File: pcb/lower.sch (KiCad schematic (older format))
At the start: 42 parts, among them J1 MALE, J10 TC2030_NL, J11 STANDOFF, J12 STANDOFF, J13 STANDOFF, J14 STANDOFF, J2 FEMALE, J3 MALE, J4 FEMALE, J5 MALE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

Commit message: 15 → 22 Ω for safety and to avoid clipping
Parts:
- R16: value 15 0.5W -> 22 0.5W; LCSC Part # C40361 -> C70404; MPN 2010W2F150JT4E -> 2010W2F220JT4S
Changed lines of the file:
@@
 P 8500 4650
 F 0 "R16" V 8295 4650 50  0000 C CNN
-F 1 "15 0.5W" V 8386 4650 50  0000 C CNN
+F 1 "22 0.5W" V 8386 4650 50  0000 C CNN
 F 2 "Resistor_SMD:R_2010_5025Metric" H 8500 4650 50  0001 C CNN
-F 3 "https://datasheet.lcsc.com/szlcsc/Uniroyal-Elec-2010W2F150JT4E_C40361.pdf" H 8500 4650 50  0001 C CNN
-F 4 "C40361" H 8500 4650 50  0001 C CNN "LCSC Part #"
-F 5 "2010W2F150JT4E" H 8500 4650 50  0001 C CNN "MPN"
+F 3 "https://datasheet.lcsc.com/szlcsc/Uniroyal-Elec-2010W2F220JT4S_C70404.pdf" H 8500 4650 50  0001 C CNN
+F 4 "C70404" H 8500 4650 50  0001 C CNN "LCSC Part #"
+F 5 "2010W2F220JT4S" H 8500 4650 50  0001 C CNN "MPN"
 F 6 "Uniroyal Elec" H 8500 4650 50  0001 C CNN "Manufacturer"
 F 7 "2010" H 8500 4650 50  0001 C CNN "Package"

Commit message: Change to parts available for JLCPCB PCBA
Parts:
- C1: value 0.1u -> 100n; LCSC Part # C60474 -> C1525; MPN CC0402KRX7R7BB104 -> CL05B104KO5NNNC; Manufacturer YAGEO -> Samsung Electro-Mechanics
- C2, C3: LCSC Part # C277478 -> C1547; MPN CC0201JRNPO9BN120 -> 0402CG120J500NT; Manufacturer YAGEO -> Guangdong Fenghua Advanced Tech
- R1, R10, R11, R12, R13, R14, R15, R2, R3, R4, R5, R6, R7, R8: LCSC Part # C114949 -> C25117; MPN RC0402JR-07470RL -> 0402WGF4700TCE; Manufacturer YAGEO -> Uniroyal Elec
- R9: LCSC Part # C102629 -> C25744; MPN RC0402JR-0710KL -> 0402WGF1002TCE; Manufacturer RALEC -> Uniroyal Elec
- Y1: Package (none) -> SMD-3225_4P

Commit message: Make fields compatible with JLCPCB BOM plugin
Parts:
- BZ1: JLCPCB BOM (none) -> False; LCSC Part (none) -> C94598; LCSC Part # C94598 -> (none)
- C1: LCSC Part (none) -> C1525; LCSC Part # C1525 -> (none)
- C2, C3: LCSC Part (none) -> C1547; LCSC Part # C1547 -> (none)
- D1, D2, D3, D4: LCSC Part (none) -> C194323; LCSC Part # C194323 -> (none)
- D5: LCSC Part (none) -> C60580; LCSC Part # C60580 -> (none)
- J1, J3, J5, J7: JLCPCB BOM (none) -> False; LCSC Part (none) -> C239333; LCSC Part # C239333 -> (none)
- J10, J11, J12, J13, J14, J9: JLCPCB BOM (none) -> False
- J2, J4, J6, J8: JLCPCB BOM (none) -> False; LCSC Part (none) -> C239353; LCSC Part # C239353 -> (none)
- Q1: LCSC Part (none) -> C8667; LCSC Part # C8667 -> (none)
- R1, R10, R11, R12, R13, R14, R15, R2, R3, R4, R5, R6, R7, R8: LCSC Part (none) -> C25117; LCSC Part # C25117 -> (none)
- R16: LCSC Part (none) -> C70404; LCSC Part # C70404 -> (none)
- R9: LCSC Part (none) -> C25744; LCSC Part # C25744 -> (none)
- U3: LCSC Part (none) -> C783592; LCSC Part # C783592 -> (none)
- Y1: LCSC Part (none) -> C12668; LCSC Part # C12668 -> (none)

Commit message: Fix: Wrong pin numbering of transistor
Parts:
- Q1: symbol Transistor_BJT:PN2222A -> node:PMBT3904
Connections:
- net GNDB: now also Q1.2 (E); no longer Q1.1 (E)
- net at R15.1: now also Q1.1 (B); no longer Q1.2 (B)
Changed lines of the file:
@@
 	8350 5100 8500 5100
 $Comp
-L Transistor_BJT:PN2222A Q1
+L node:PMBT3904 Q1
 U 1 1 5F9890BA
 P 8400 5500

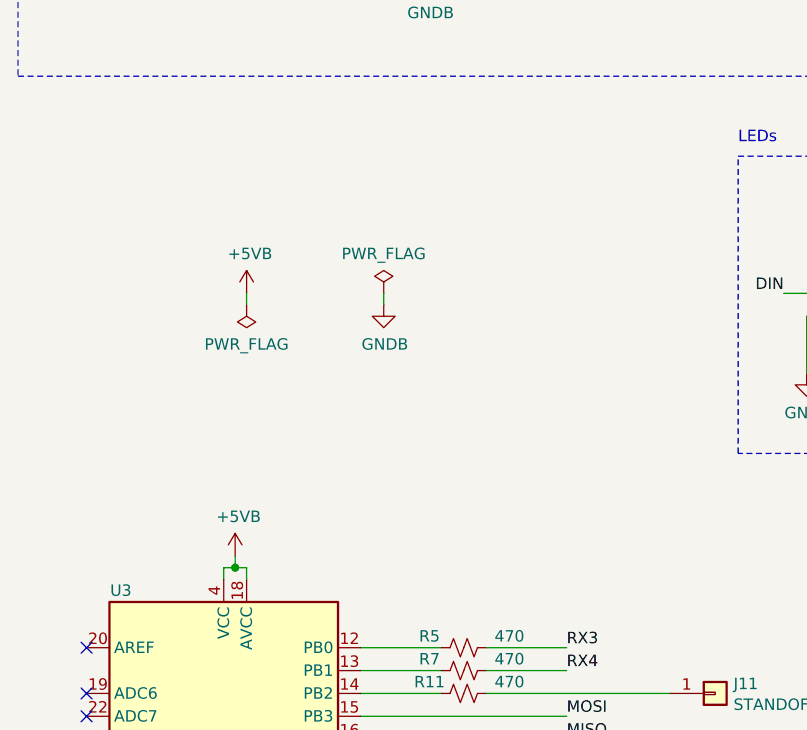
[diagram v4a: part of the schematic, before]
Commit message: Specify and wire up Schottky diode
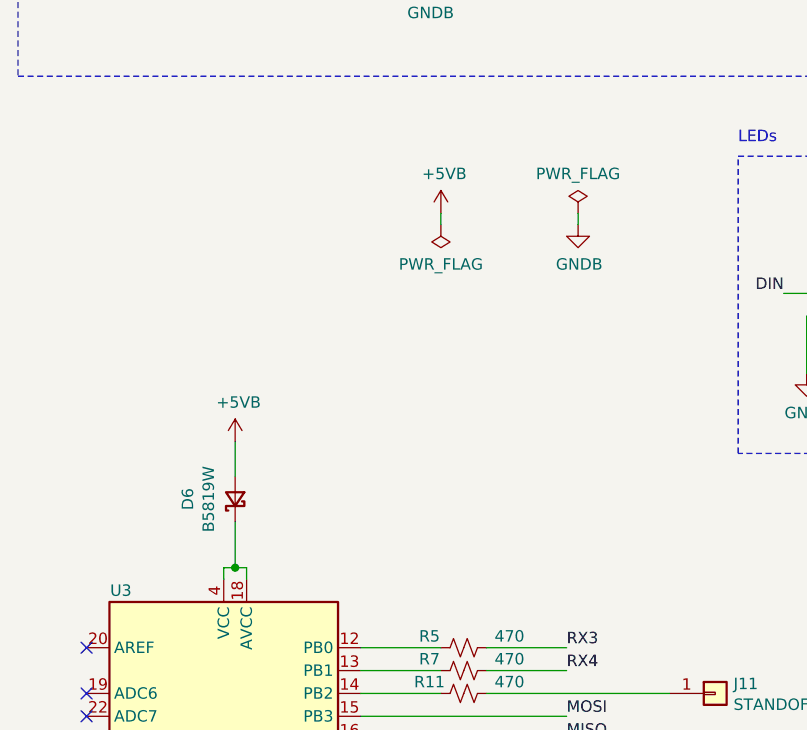
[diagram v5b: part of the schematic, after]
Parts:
- added D6: B5819W, Diode_SMD:D_SOD-123, symbol Device:D_Schottky_Small
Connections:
- net +5VB: now also D6.2 (A); no longer U3.18 (AVCC), U3.4 (VCC), U3.6 (VCC)
- new net: D6.1 (K), U3.18 (AVCC), U3.4 (VCC), U3.6 (VCC)
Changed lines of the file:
@@
 RX4
-Wire Wire Line
-	1550 4300 1550 4350
 Wire Wire Line
 	2450 4900 2100 4900
@@
 L node:+5VB #PWR0101
 U 1 1 5F8748FF
-P 1550 4300
-F 0 "#PWR0101" H 1550 4150 50  0001 C CNN
-F 1 "+5VB" H 1565 4473 50  0000 C CNN
-F 2 "" H 1550 4300 50  0001 C CNN
-F 3 "" H 1550 4300 50  0001 C CNN
-	1    1550 4300
+P 1550 3800
+F 0 "#PWR0101" H 1550 3650 50  0001 C CNN
+F 1 "+5VB" H 1565 3973 50  0000 C CNN
+F 2 "" H 1550 3800 50  0001 C CNN
+F 3 "" H 1550 3800 50  0001 C CNN
+	1    1550 3800
 	1    0    0    -1
 $EndComp
@@
 L power:PWR_FLAG #FLG0101
 U 1 1 5F887FE3
-P 2200 3150
-F 0 "#FLG0101" H 2200 3225 50  0001 C CNN
-F 1 "PWR_FLAG" H 2200 3323 50  0000 C CNN
-F 2 "" H 2200 3150 50  0001 C CNN
-F 3 "~" H 2200 3150 50  0001 C CNN
-	1    2200 3150
+P 3050 2800
+F 0 "#FLG0101" H 3050 2875 50  0001 C CNN
+F 1 "PWR_FLAG" H 3050 2973 50  0000 C CNN
+F 2 "" H 3050 2800 50  0001 C CNN
+F 3 "~" H 3050 2800 50  0001 C CNN
+	1    3050 2800
 	1    0    0    -1
 $EndComp
@@
 L node:+5VB #PWR0128
 U 1 1 5F888530
-P 1600 3150
-F 0 "#PWR0128" H 1600 3000 50  0001 C CNN
-F 1 "+5VB" H 1615 3323 50  0000 C CNN
-F 2 "" H 1600 3150 50  0001 C CNN
-F 3 "" H 1600 3150 50  0001 C CNN
-	1    1600 3150
+P 2450 2800
+F 0 "#PWR0128" H 2450 2650 50  0001 C CNN
+F 1 "+5VB" H 2465 2973 50  0000 C CNN
+F 2 "" H 2450 2800 50  0001 C CNN
+F 3 "" H 2450 2800 50  0001 C CNN
+	1    2450 2800
 	1    0    0    -1
 $EndComp
@@
 L node:GNDB #PWR0129
 U 1 1 5F88863E
-P 2200 3200
-F 0 "#PWR0129" H 2200 2950 50  0001 C CNN
-F 1 "GNDB" H 2205 3027 50  0000 C CNN
-F 2 "" H 2200 3200 50  0001 C CNN
-F 3 "" H 2200 3200 50  0001 C CNN
-	1    2200 3200
+P 3050 2850
+F 0 "#PWR0129" H 3050 2600 50  0001 C CNN
+F 1 "GNDB" H 3055 2677 50  0000 C CNN
+F 2 "" H 3050 2850 50  0001 C CNN
+F 3 "" H 3050 2850 50  0001 C CNN
+	1    3050 2850
 	1    0    0    -1
 $EndComp
@@
 L power:PWR_FLAG #FLG0102
 U 1 1 5F8888F9
-P 1600 3200
-F 0 "#FLG0102" H 1600 3275 50  0001 C CNN
-F 1 "PWR_FLAG" H 1600 3373 50  0000 C CNN
-F 2 "" H 1600 3200 50  0001 C CNN
-F 3 "~" H 1600 3200 50  0001 C CNN
-	1    1600 3200
+P 2450 2850
+F 0 "#FLG0102" H 2450 2925 50  0001 C CNN
+F 1 "PWR_FLAG" H 2450 3023 50  0000 C CNN
+F 2 "" H 2450 2850 50  0001 C CNN
+F 3 "~" H 2450 2850 50  0001 C CNN
+	1    2450 2850
 	-1   0    0    1
 $EndComp
 Wire Wire Line
-	1600 3150 1600 3200
-Wire Wire Line
-	2200 3150 2200 3200
+	2450 2800 2450 2850
+Wire Wire Line
+	3050 2800 3050 2850
 $Comp
 L Connector_Generic:Conn_01x01 J11
@@
 	6900 1750 7400 1750
 Connection ~ 6900 1150
+$Comp
+L Device:D_Schottky_Small D6
+U 1 1 5FC11A77
+P 1550 4050
+F 0 "D6" H 1550 4257 50  0000 C CNN
+F 1 "B5819W" H 1550 4166 50  0000 C CNN
+F 2 "Diode_SMD:D_SOD-123" V 1550 4050 50  0001 C CNN
+F 3 "~" V 1550 4050 50  0001 C CNN
+	1    1550 4050
+	0    -1   -1   0
+$EndComp
+Wire Wire Line
+	1550 4150 1550 4350
+Wire Wire Line
+	1550 3950 1550 3800
 $EndSCHEMATC

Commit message: Fix bridging: Move male headers to upper board
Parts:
- removed J1, J3, J5, J7: MALE, Connector_PinHeader_2.54mm:PinHeader_2x02_P2.54mm_Horizontal, symbol Connector_Generic:Conn_02x02_Top_Bottom
- J2, J4, J6, J8: symbol Connector_Generic:Conn_02x02_Odd_Even -> Connector_Generic:Conn_02x02_Top_Bottom
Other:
- note removed: "1234 in 3D model: male YBRG, female BGYR"
- moved on the sheet: J2, J4, J6, J8

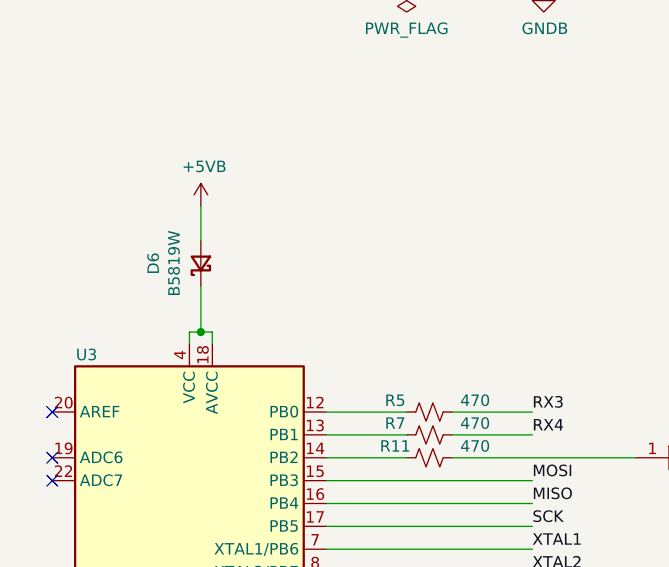
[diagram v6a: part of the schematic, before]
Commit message: Add missing power flag
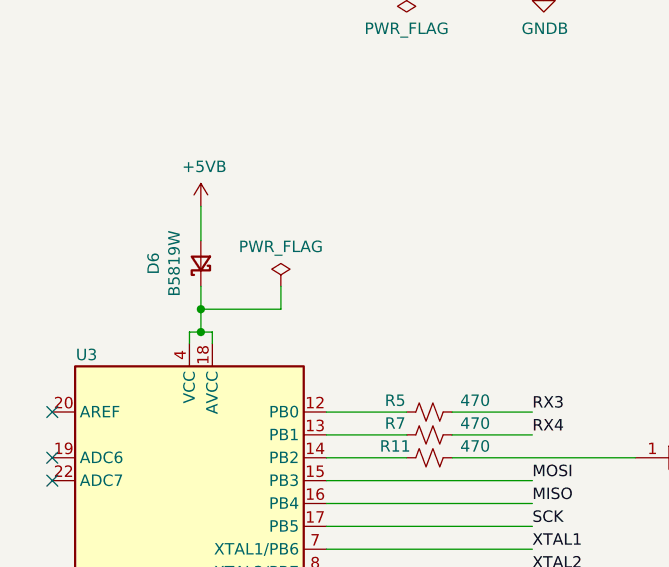
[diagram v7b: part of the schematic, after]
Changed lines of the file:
@@
 $EndComp
 Wire Wire Line
-	1550 4150 1550 4350
+	1550 4150 1550 4250
 Wire Wire Line
 	1550 3950 1550 3800
@@
 Wire Wire Line
 	5800 1300 5900 1300
+$Comp
+L power:PWR_FLAG #FLG0105
+U 1 1 5FDE68E6
+P 1900 4150
+F 0 "#FLG0105" H 1900 4225 50  0001 C CNN
+F 1 "PWR_FLAG" H 1900 4323 50  0000 C CNN
+F 2 "" H 1900 4150 50  0001 C CNN
+F 3 "~" H 1900 4150 50  0001 C CNN
+	1    1900 4150
+	1    0    0    -1
+$EndComp
+Wire Wire Line
+	1550 4250 1900 4250
+Wire Wire Line
+	1900 4250 1900 4150
+Connection ~ 1550 4250
+Wire Wire Line
+	1550 4250 1550 4350
 $EndSCHEMATC
